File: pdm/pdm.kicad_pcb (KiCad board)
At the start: 4 copper layers, 129.5 x 99.1 mm, 111 parts, among them J1 Conn_01x04_Male, J2 Conn_01x12_Male, J3 Conn_01x08_Male, Q1 MMBT3904, Q10 Q_NPN_BCE, Q2 Q_NPN_BCE, Q3 MMBT3904, Q4 Q_NPN_BCE, Q5 MMBT3904, Q6 Q_NPN_BCE, Q7 MMBT3904, Q8 Q_NPN_BCE, Q9 MMBT3904, SW1 SW_Push, U1 AZ1117CH-3_3TRG1, U2 SN65HVD233, U3 STM32F042G6Ux, U4 BTS443P, U5 BTS443P, U6 BTS443P, U7 BTS443P, U8 BTS443P

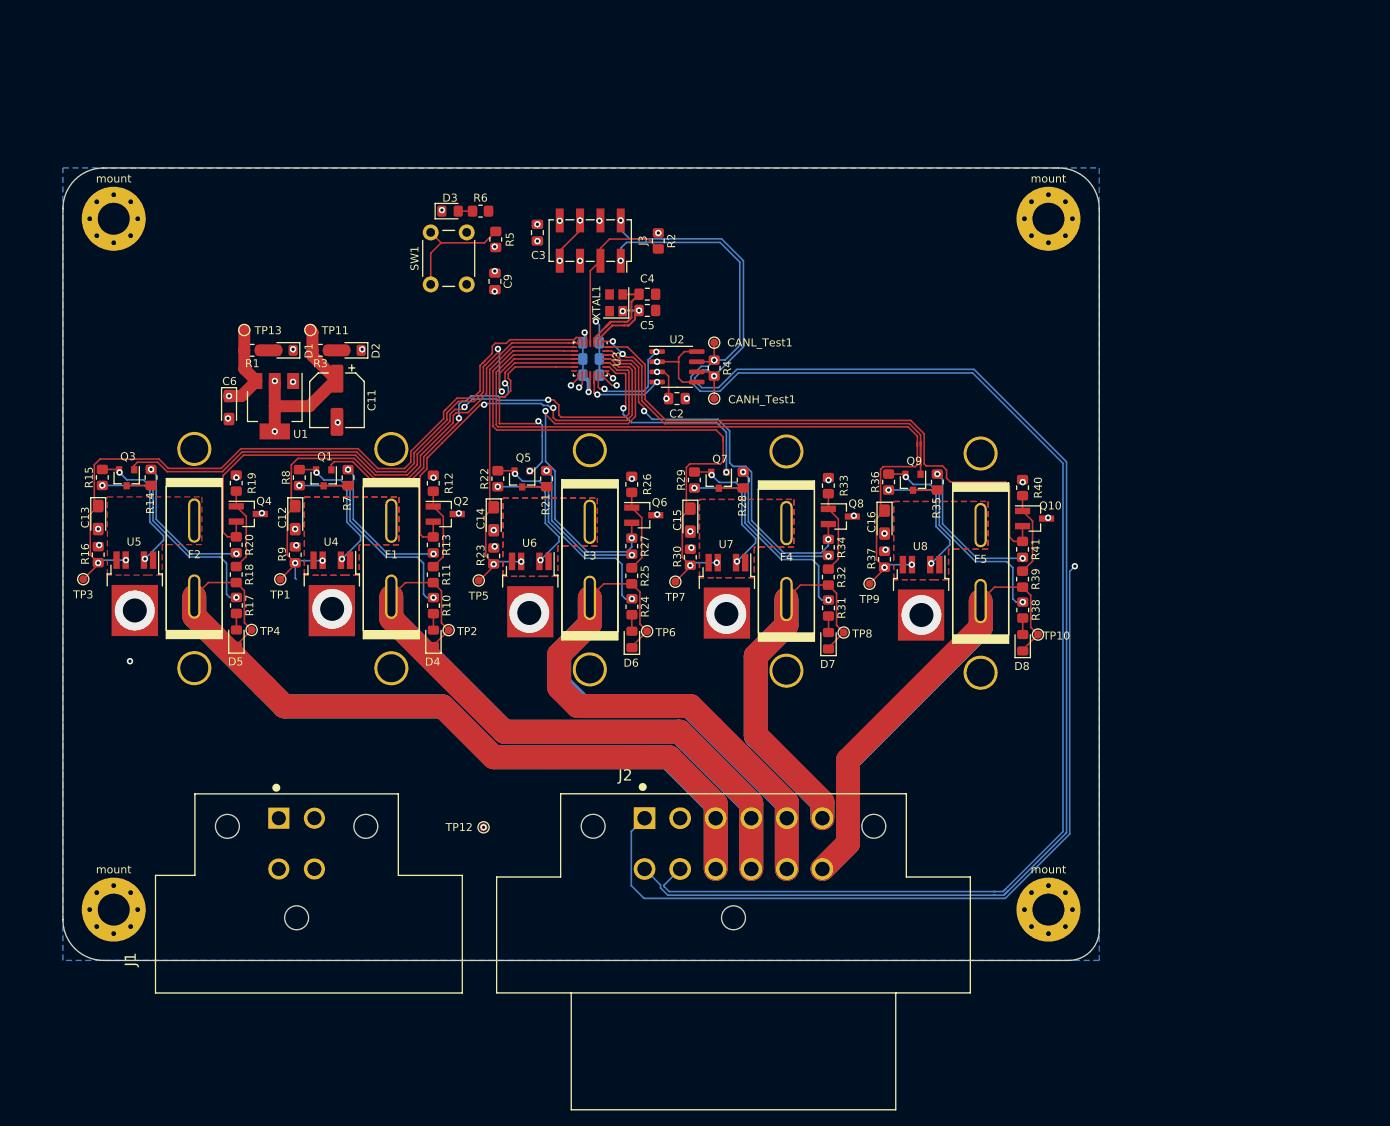
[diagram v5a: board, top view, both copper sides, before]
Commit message: added pin mappings
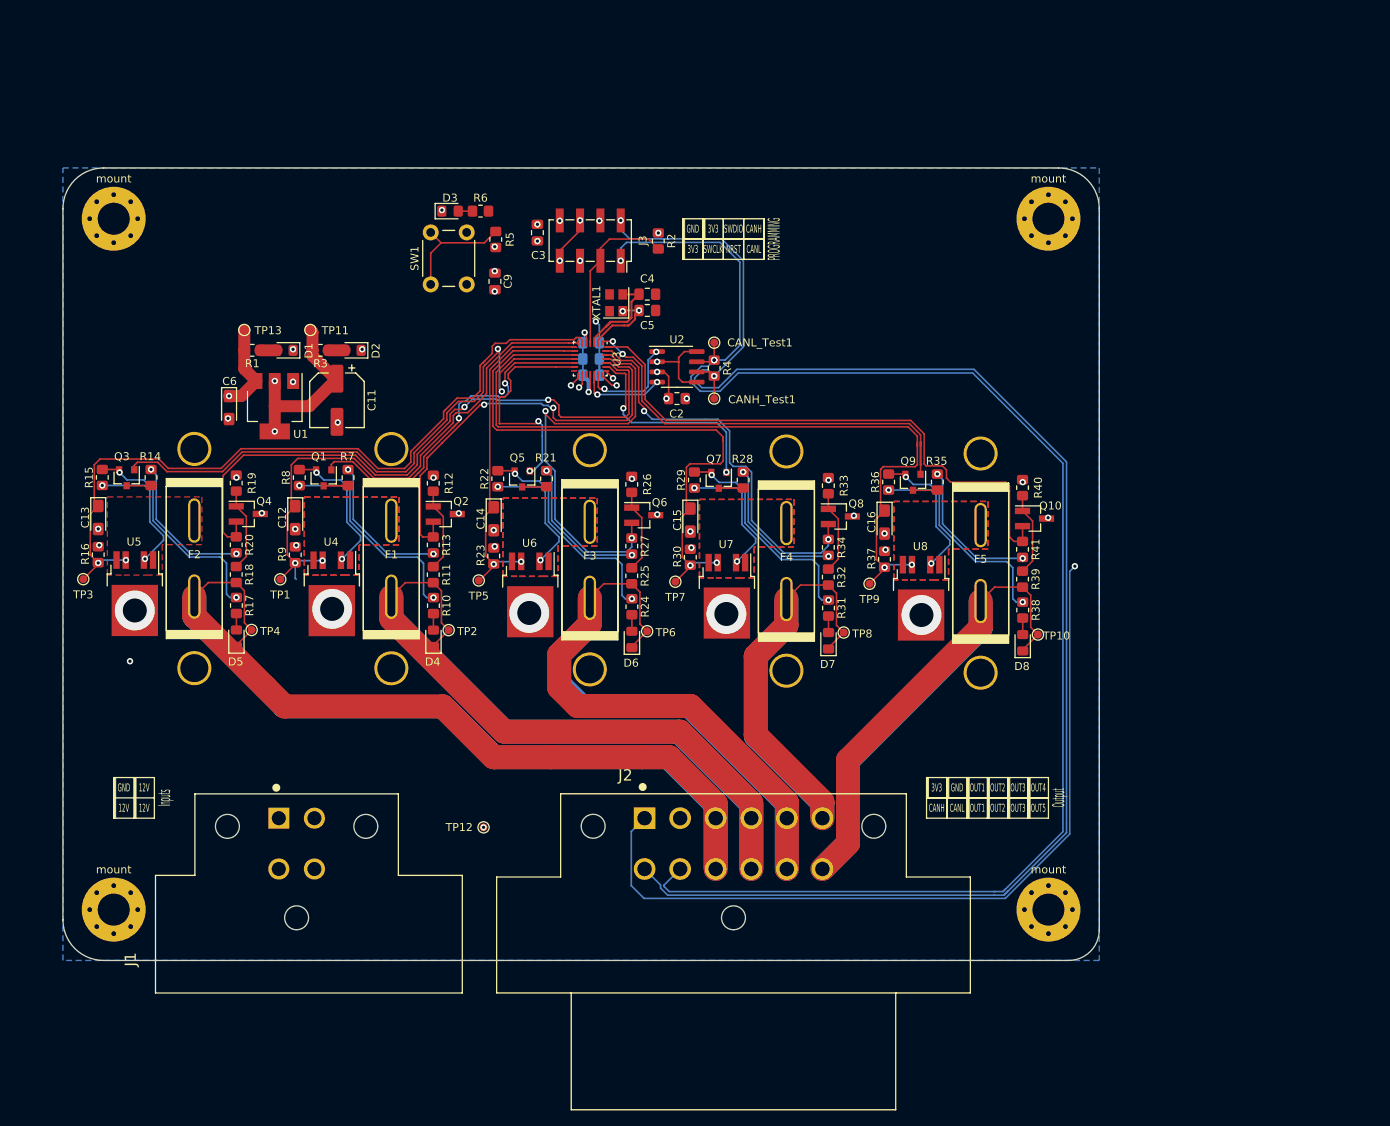
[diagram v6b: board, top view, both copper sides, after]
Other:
- board text added: "12V"
- board text added: "3V3"
- board text added: "CANH"
- board text added: "CANL"
- board text added: "GND"
- board text added: "Inputs"
- board text added: "NRST"
- board text added: "OUT1"
- board text added: "OUT2"
- board text added: "OUT3"
- board text added: "OUT4"
- board text added: "OUT5"
- board text added: "Output"
- board text added: "PROGRAMMING"
- board text added: "SWCLK"
- board text added: "SWDIO"

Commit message: added mounting holes again
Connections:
- R6 pad 2: (no net) -> /LED_DEBUG
- U3 pad 14: (no net) -> /LED_DEBUG
- U3 pad 17: (no net) -> +3V3
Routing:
- net /LED_DEBUG: track 0.00 -> 31.5 mm, vias 0 -> 2
- net /DEBUG_BUTTON: track 40.1 -> 43.4 mm
- net Net-(C4-Pad1): track 0.00 -> 2.03 mm
- net +3V3: track 239.5 -> 240.0 mm

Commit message: fixed labelling
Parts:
- removed TP10: TestPoint_Probe, TestPoint:TestPoint_Pad_D1.0mm
- removed mount (x4): MountingHole_4mm_Pad_Via, MountingHole:MountingHole_4mm_Pad_Via
- added Vout_TP1: TestPoint_Probe, TestPoint:TestPoint_Pad_D1.0mm, F.Cu at (226.1, 99.2)
- CANH_TP1: renamed from CANH_Test1; value CANH_TEST -> CANH_Test1
- CANL_Test1: value CANL_TEST -> CANL_TP
- renumbered TP11 to 3V3_TP1, TP12 to GND_TP1, TP9 to Sense_TP1, TP13 to Vin_TP1
